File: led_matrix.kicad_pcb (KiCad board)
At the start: 2 copper layers, 85.1 x 109.2 mm, 116 parts, among them J1 I2C, J2 Extra, J3 Address, J4 +5V, J5 GND, J6 Power Input, J7 Columns, J8 Row Addr., Q1 2N3904, Q2 2N3904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

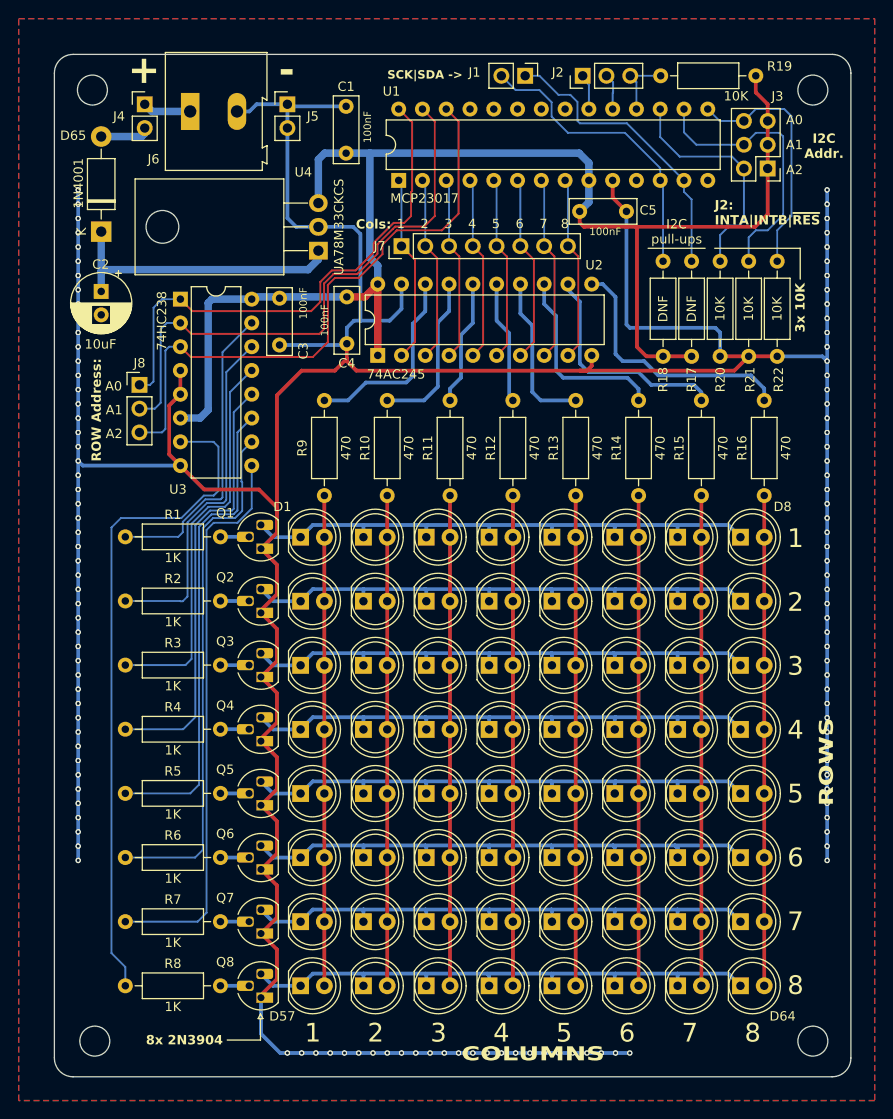
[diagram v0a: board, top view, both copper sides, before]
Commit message: Further adjustments to silkscreen
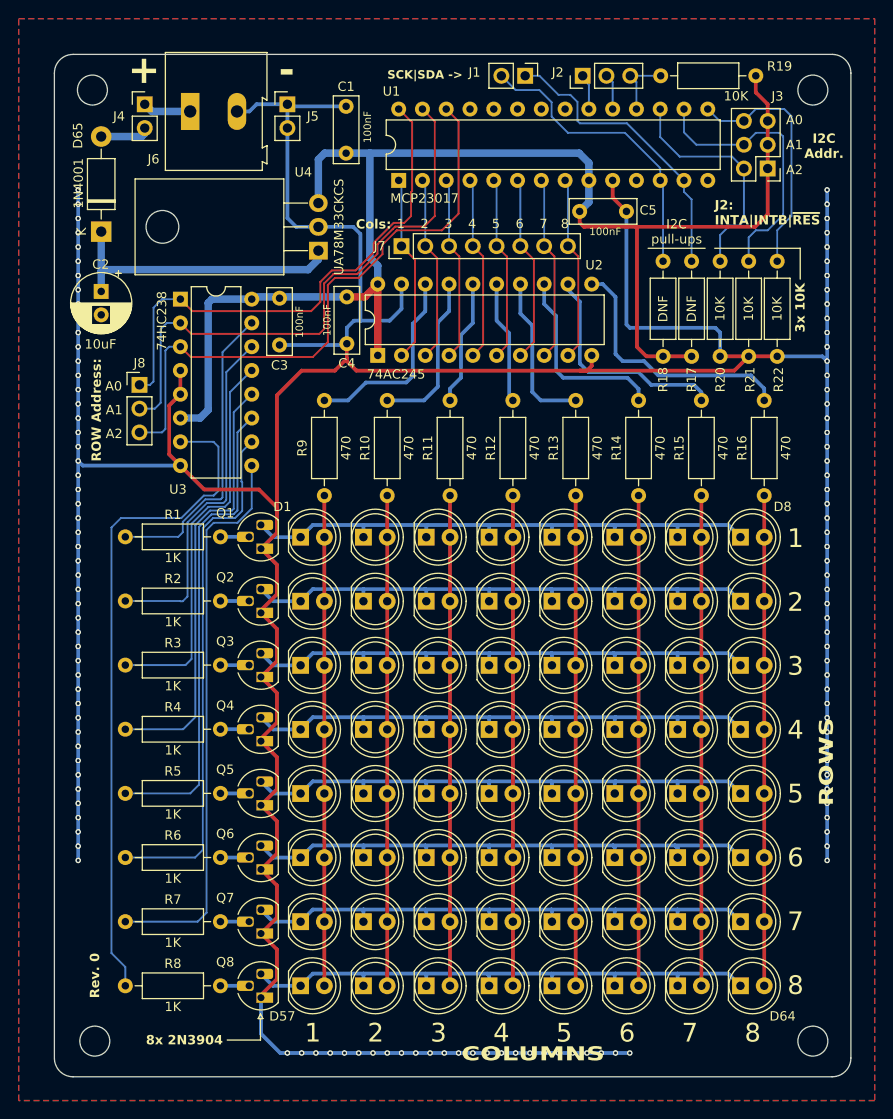
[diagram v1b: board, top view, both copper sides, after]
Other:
- board text added: "Rev. 0"
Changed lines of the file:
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@@
 		(tags "C Disc series Radial pin pitch 5.00mm  diameter 7mm width 2.5mm Capacitor")
 		(property "Reference" "C3"
-			(at 5.625572 -2.54 90)
+			(at 7.1628 0 180)
 			(layer "F.SilkS")
 			(effects
@@
 		)
 		(property "Value" "100nF"
-			(at 0.545572 -2.54 90)
+			(at 2.54 -2.1336 90)
 			(layer "F.SilkS")
 			(effects
@@
 		(tags "Diode DO-41_SOD81 series Axial Horizontal pin pitch 10.16mm  length 5.2mm diameter 2.7mm")
 		(property "Reference" "D65"
-			(at 10.2616 -2.9972 180)
+			(at 10.2616 -2.4892 -90)
 			(layer "F.SilkS")
 			(effects
@@
 		)
 		(property "Value" "100nF"
-			(at 2.5 2.363572 90)
+			(at 2.475086 2.109572 90)
 			(layer "F.SilkS")
 			(effects
@@
 		)
 	)
+	(gr_text "Rev. 0"
+		(at 104.471572 143.8656 90)
+		(layer "F.SilkS")
+		(effects
+			(font
+				(size 1 1)
+				(thickness 0.2)
+				(bold yes)
+			)
+			(justify left)
+		)
+	)
 	(gr_text "7"
 		(at 152.4 61.722 0)
@@
 	)
 	(segment
-		(start 159.843572 47.105714)
-		(end 159.792772 47.156514)
-		(width 0.2)
-		(layer "B.Cu")
-		(net 24)
-	)
-	(segment
-		(start 159.843572 46.038914)
-		(end 159.843572 47.105714)
-		(width 0.2)
-		(layer "B.Cu")
-		(net 24)
-	)
-	(segment
-		(start 159.792772 47.156514)
-		(end 159.792772 48.883714)
+		(start 159.792772 48.883714)
+		(end 159.792772 45.988114)
 		(width 0.2)
 		(layer "B.Cu")
@@
 	)
 	(segment
-		(start 159.132372 45.327714)
-		(end 159.843572 46.038914)
+		(start 159.792772 45.988114)
+		(end 159.132372 45.327714)
 		(width 0.2)
 		(layer "B.Cu")

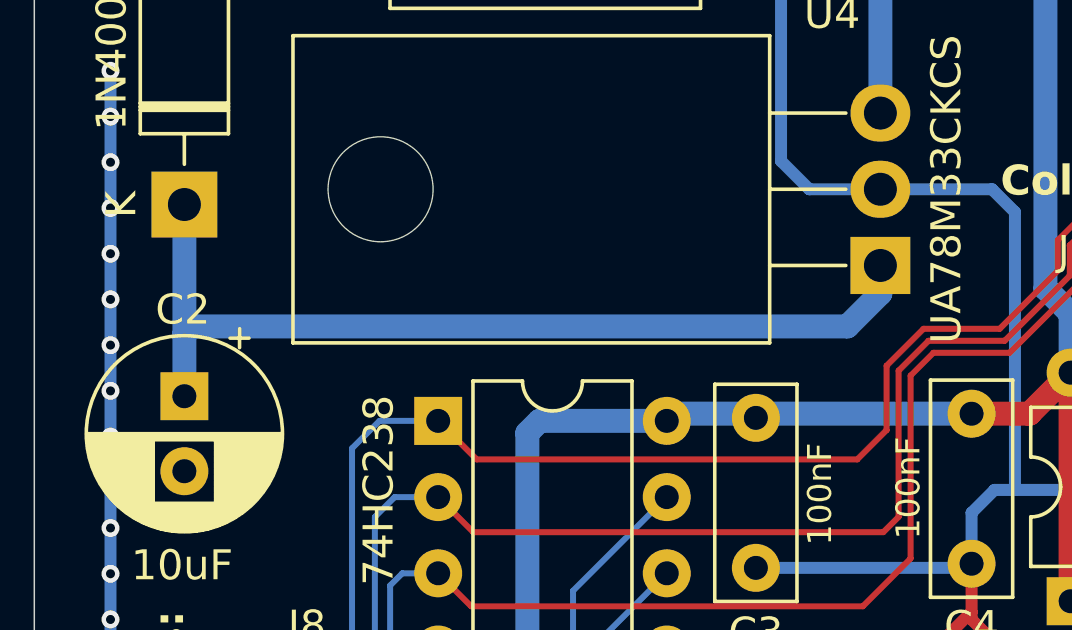
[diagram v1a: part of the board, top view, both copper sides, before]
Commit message: Update the silkcreen and solder mask
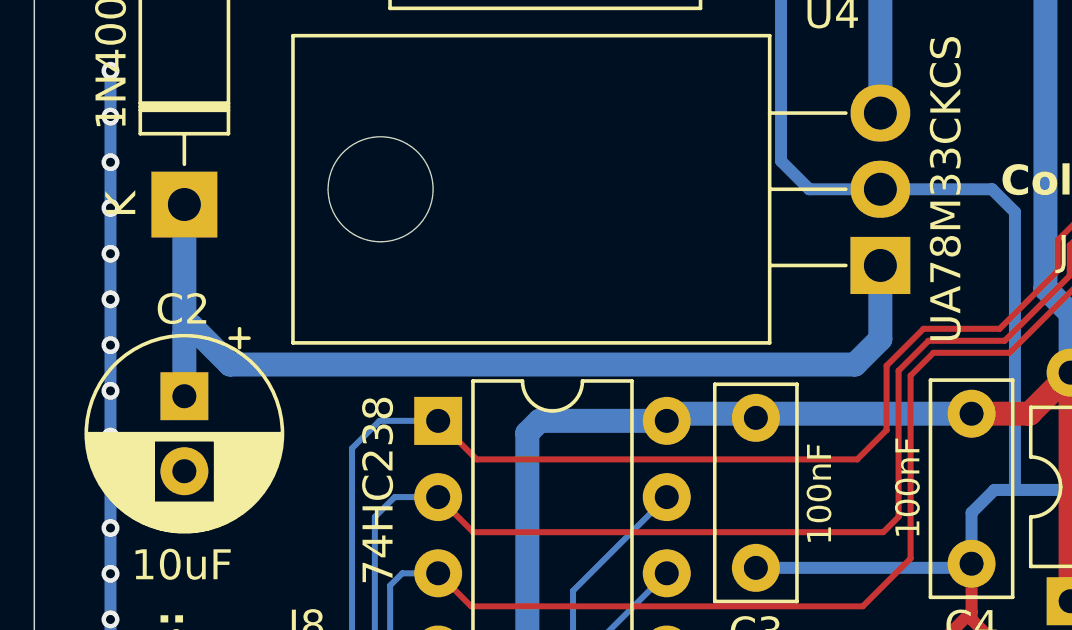
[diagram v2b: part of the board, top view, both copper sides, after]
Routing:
- net /RECT_5V: track 31.1 -> 33.0 mm
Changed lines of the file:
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@@
 	)
 	(segment
-		(start 128.356 64.938)
-		(end 127.254 66.04)
+		(start 128.356 66.462)
+		(end 127.508 67.31)
+		(width 0.8)
+		(layer "B.Cu")
+		(net 70)
+	)
+	(segment
+		(start 105.41 66.04)
+		(end 105.156 66.294)
+		(width 0.8)
+		(layer "B.Cu")
+		(net 70)
+	)
+	(segment
+		(start 106.68 67.31)
+		(end 105.41 66.04)
 		(width 0.8)
 		(layer "B.Cu")
@@
 	)
 	(segment
-		(start 127.254 66.04)
-		(end 105.41 66.04)
+		(start 127.508 67.31)
+		(end 106.68 67.31)
 		(width 0.8)
 		(layer "B.Cu")
@@
 	(segment
 		(start 128.356 64.008)
-		(end 128.356 64.938)
-		(width 0.8)
-		(layer "B.Cu")
-		(net 70)
-	)
-	(segment
-		(start 105.41 66.04)
-		(end 105.156 66.294)
+		(end 128.356 66.462)
 		(width 0.8)
 		(layer "B.Cu")
@@
 			)
 		)
+	)
+	(zone
+		(net 0)
+		(net_name "")
+		(layer "B.Mask")
+		(hatch edge 0.5)
+		(connect_pads
+			(clearance 0.5)
+		)
+		(min_thickness 0.25)
+		(filled_areas_thickness no)
+		(fill yes
+			(thermal_gap 0.5)
+			(thermal_bridge_width 0.5)
+		)
+		(polygon
+			(pts
+				(xy 109.22 59.182) (xy 114.038 59.182) (xy 114.038 63.754) (xy 109.22 63.754)
+			)
+		)

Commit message: reorganize some traces
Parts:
- moved C5 1.04 mm to (157.3, 59.8)
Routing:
- net GND: track 455.6 -> 488.4 mm, vias 121 -> 141
- net VCC: track 152.0 -> 150.5 mm
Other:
- board text added: "4.5V to 8V DC ONLY!!!"
- board text added: "8x8 LED MATRIX EDUBOARD"
- board text added: "SCK|SDA"
- board text removed: "SCK|SDA ->"

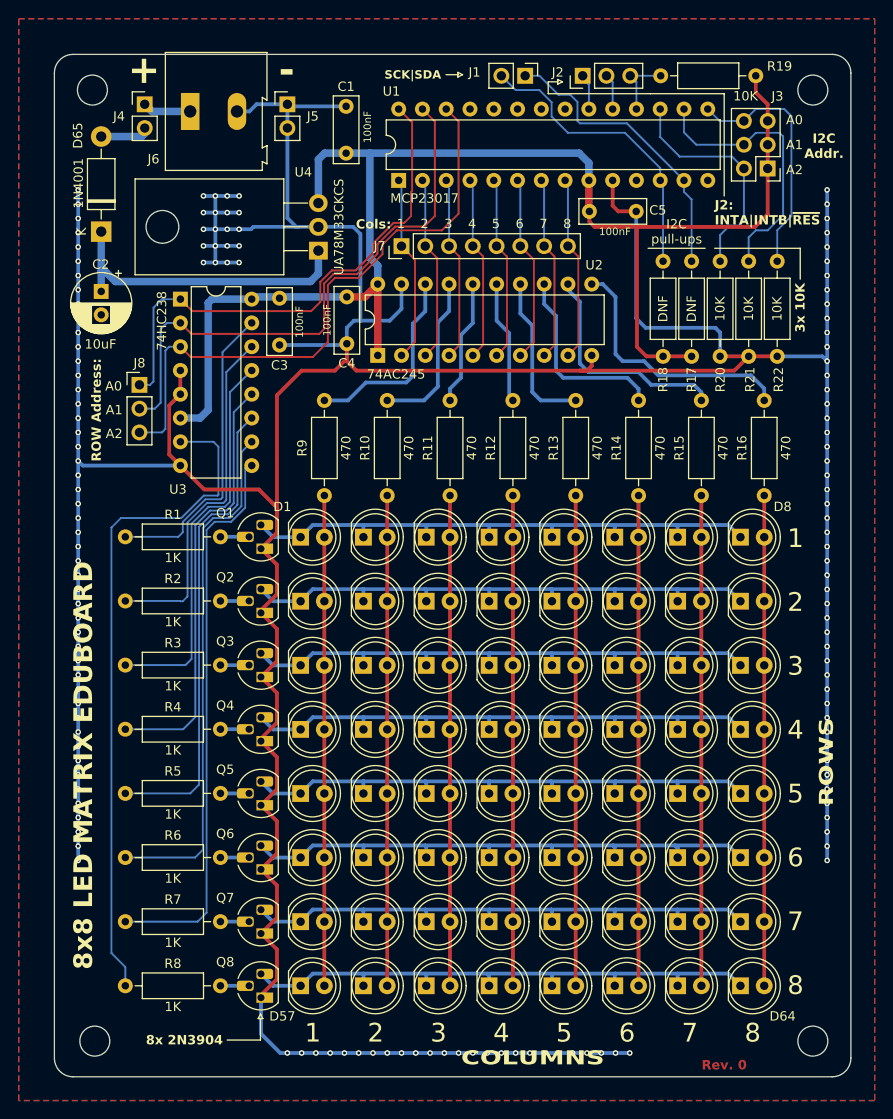
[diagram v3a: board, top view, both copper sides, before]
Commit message: Enlarge mounting holes
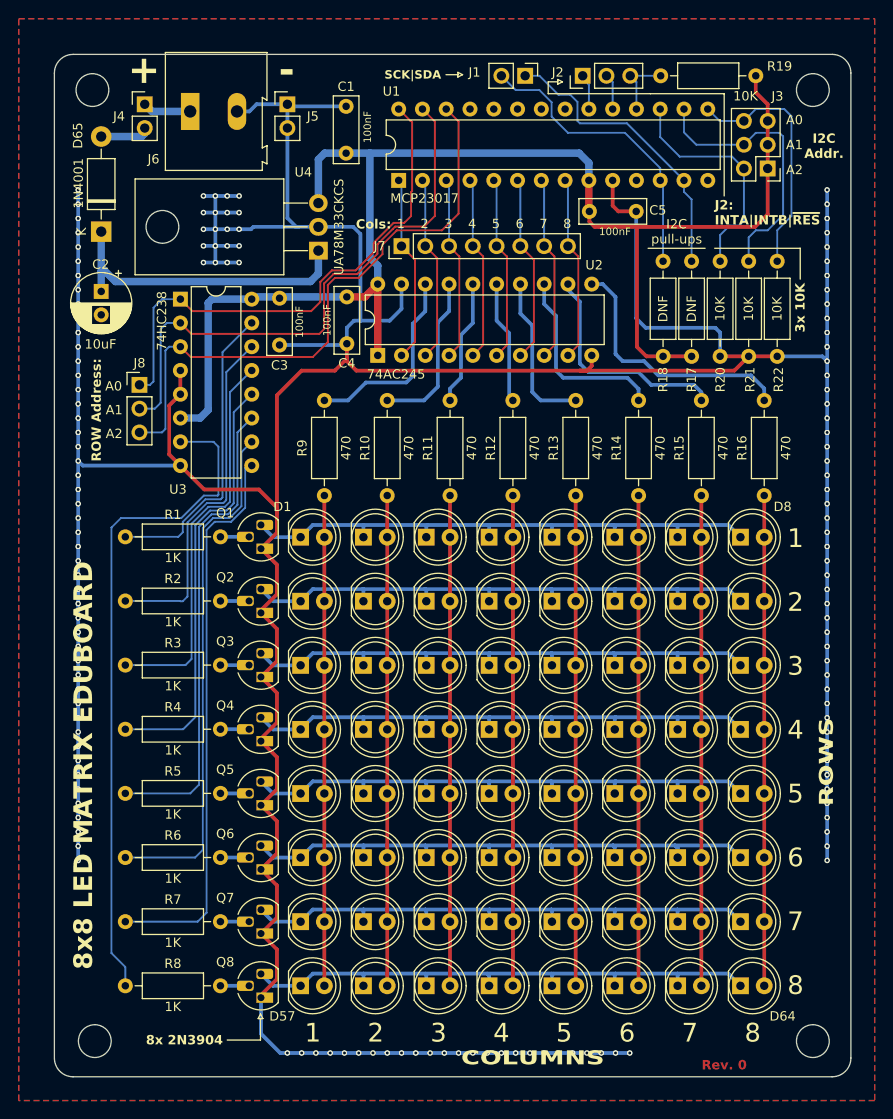
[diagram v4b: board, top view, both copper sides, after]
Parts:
- H1, H2, H3, H4: footprint MountingHole:MountingHole_3.2mm_M3_DIN965 -> MountingHole:MountingHole_3.5mm
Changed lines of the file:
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@@
 		)
 	)
-	(footprint "MountingHole:MountingHole_3.2mm_M3_DIN965"
+	(footprint "MountingHole:MountingHole_3.5mm"
 		(layer "F.Cu")
 		(at 181.179572 148.451714)
-		(descr "Mounting Hole 3.2mm, no annular, M3, DIN965")
-		(tags "mounting hole 3.2mm no annular m3 din965")
+		(descr "Mounting Hole 3.5mm, no annular")
+		(tags "mounting hole 3.5mm no annular")
 		(property "Reference" "H2"
-			(at 0 -3.8 0)
+			(at 0 -4.5 0)
 			(layer "F.SilkS")
 			(hide yes)
@@
 		)
 		(property "Value" "MountingHole"
-			(at 0 3.8 0)
+			(at 0 4.5 0)
 			(layer "F.Fab")
 			(effects
@@
 			)
 		)
-		(property "Footprint" "MountingHole:MountingHole_3.2mm_M3_DIN965"
+		(property "Footprint" "MountingHole:MountingHole_3.5mm"
 			(at 0 0 0)
 			(unlocked yes)
@@
 		(fp_circle
 			(center 0 0)
-			(end 2.8 0)
+			(end 3.5 0)
 			(stroke
 				(width 0.15)
@@
 		(fp_circle
 			(center 0 0)
-			(end 3.05 0)
+			(end 3.75 0)
 			(stroke
 				(width 0.05)
@@
 		(pad "" np_thru_hole circle
 			(at 0 0)
-			(size 3.2 3.2)
-			(drill 3.2)
+			(size 3.5 3.5)
+			(drill 3.5)
 			(layers "*.Cu" "*.Mask")
 		)
@@
 		)
 	)
-	(footprint "MountingHole:MountingHole_3.2mm_M3_DIN965"
+	(footprint "MountingHole:MountingHole_3.5mm"
 		(layer "F.Cu")
 		(at 181.179572 46.851714)
-		(descr "Mounting Hole 3.2mm, no annular, M3, DIN965")
-		(tags "mounting hole 3.2mm no annular m3 din965")
+		(descr "Mounting Hole 3.5mm, no annular")
+		(tags "mounting hole 3.5mm no annular")
 		(property "Reference" "H3"
-			(at 0 -3.8 0)
+			(at 0 -4.5 0)
 			(layer "F.SilkS")
 			(hide yes)
@@
 		)
 		(property "Value" "MountingHole"
-			(at 0 3.8 0)
+			(at 0 4.5 0)
 			(layer "F.Fab")
 			(effects
@@
 			)
 		)
-		(property "Footprint" "MountingHole:MountingHole_3.2mm_M3_DIN965"
+		(property "Footprint" "MountingHole:MountingHole_3.5mm"
 			(at 0 0 0)
 			(unlocked yes)
@@
 		(fp_circle
 			(center 0 0)
-			(end 2.8 0)
+			(end 3.5 0)
 			(stroke
 				(width 0.15)
@@
 		(fp_circle
 			(center 0 0)
-			(end 3.05 0)
+			(end 3.75 0)
 			(stroke
 				(width 0.05)
@@
 		(pad "" np_thru_hole circle
 			(at 0 0)
-			(size 3.2 3.2)
-			(drill 3.2)
+			(size 3.5 3.5)
+			(drill 3.5)
 			(layers "*.Cu" "*.Mask")
 		)
@@
 		)
 	)
-	(footprint "MountingHole:MountingHole_3.2mm_M3_DIN965"
+	(footprint "MountingHole:MountingHole_3.5mm"
 		(layer "F.Cu")
 		(at 104.471572 148.451714)
-		(descr "Mounting Hole 3.2mm, no annular, M3, DIN965")
-		(tags "mounting hole 3.2mm no annular m3 din965")
+		(descr "Mounting Hole 3.5mm, no annular")
+		(tags "mounting hole 3.5mm no annular")
 		(property "Reference" "H1"
-			(at 0 -3.8 0)
+			(at 0 -4.5 0)
 			(layer "F.SilkS")
 			(hide yes)
@@
 		)
 		(property "Value" "MountingHole"
-			(at 0 3.8 0)
+			(at 0 4.5 0)
 			(layer "F.Fab")
 			(effects
@@
 			)
 		)
-		(property "Footprint" "MountingHole:MountingHole_3.2mm_M3_DIN965"
+		(property "Footprint" "MountingHole:MountingHole_3.5mm"
 			(at 0 0 0)
 			(unlocked yes)
@@
 		(fp_circle
 			(center 0 0)
-			(end 2.8 0)
+			(end 3.5 0)
 			(stroke
 				(width 0.15)
@@
 		(fp_circle
 			(center 0 0)
-			(end 3.05 0)
+			(end 3.75 0)
 			(stroke
 				(width 0.05)
@@
 		(pad "" np_thru_hole circle
 			(at 0 0)
-			(size 3.2 3.2)
-			(drill 3.2)
+			(size 3.5 3.5)
+			(drill 3.5)
 			(layers "*.Cu" "*.Mask")
 		)
@@
 		)
 	)
-	(footprint "MountingHole:MountingHole_3.2mm_M3_DIN965"
+	(footprint "MountingHole:MountingHole_3.5mm"
 		(layer "F.Cu")
 		(at 104.217572 46.851714)
-		(descr "Mounting Hole 3.2mm, no annular, M3, DIN965")
-		(tags "mounting hole 3.2mm no annular m3 din965")
+		(descr "Mounting Hole 3.5mm, no annular")
+		(tags "mounting hole 3.5mm no annular")
 		(property "Reference" "H4"
-			(at 0 -3.8 0)
+			(at 0 -4.5 0)
 			(layer "F.SilkS")
 			(hide yes)
@@
 		)
 		(property "Value" "MountingHole"
-			(at 0 3.8 0)
+			(at 0 4.5 0)
 			(layer "F.Fab")
 			(effects
@@
 			)
 		)
-		(property "Footprint" "MountingHole:MountingHole_3.2mm_M3_DIN965"
+		(property "Footprint" "MountingHole:MountingHole_3.5mm"
 			(at 0 0 0)
 			(unlocked yes)
@@
 		(fp_circle
 			(center 0 0)
-			(end 2.8 0)
+			(end 3.5 0)
 			(stroke
 				(width 0.15)
@@
 		(fp_circle
 			(center 0 0)
-			(end 3.05 0)
+			(end 3.75 0)
 			(stroke
 				(width 0.05)
@@
 		(pad "" np_thru_hole circle
 			(at 0 0)
-			(size 3.2 3.2)
-			(drill 3.2)
+			(size 3.5 3.5)
+			(drill 3.5)
 			(layers "*.Cu" "*.Mask")
 		)

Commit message: Update silkscreen
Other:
- board text added: "R O W S"
- board text removed: "ROWS"
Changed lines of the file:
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@@
 		)
 	)
-	(gr_text "ROWS"
-		(at 182.626 118.618 90)
+	(gr_text "R\nO\nW\nS"
+		(at 182.626 118.618 0)
 		(layer "F.SilkS")
 		(effects
